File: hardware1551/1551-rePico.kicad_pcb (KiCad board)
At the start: 2 copper layers, 64.1 x 99.4 mm, 41 parts, among them J1 0.96_I2C_OLED, J10 TCBM, J11 JTAG, J6 Conn_01x05, J8 SD CARD, Q1 BSS138, Q2 BSS138, Q3 BSS138, Q4 BSS138, U1 Pico, U3 XC9572XL-VQ64, U4 6523 (pins), U5 6510T (pins), U6 6510T (socket for chip)

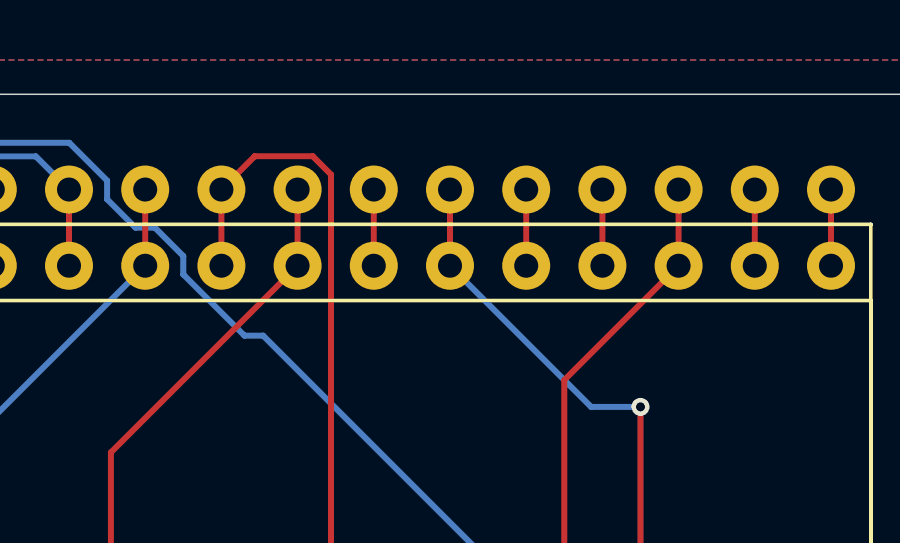
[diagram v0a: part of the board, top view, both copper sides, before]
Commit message: disconnect WPS from mainboard WPS becuase it's an output of U8 (pin2) that will keep it low with no mechanism present
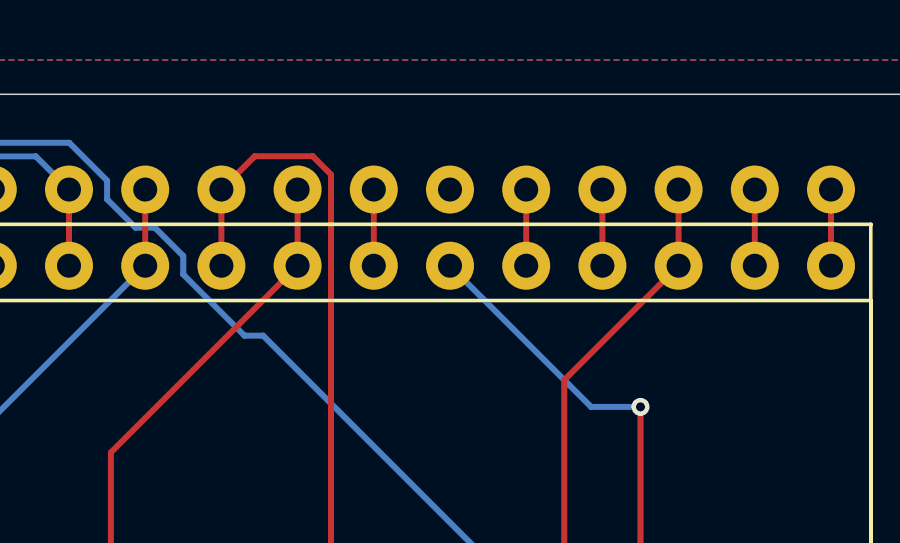
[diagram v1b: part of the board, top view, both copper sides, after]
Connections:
- U5 pad 26: /WPS -> unconnected-(U5-P4-Pad26)
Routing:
- net /WPS: track 40.9 -> 38.3 mm
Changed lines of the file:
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@@
 	(net 121 "Net-(JP5-A)")
 	(net 122 "/~{IRQ_BRD}")
+	(net 123 "unconnected-(U5-P4-Pad26)")
 	(footprint "Jumper:SolderJumper-3_P1.3mm_Bridged12_RoundedPad1.0x1.5mm_NumberLabels"
 		(layer "F.Cu")
@@
 			(layers "*.Cu" "*.Mask")
 			(remove_unused_layers no)
-			(net 41 "/WPS")
+			(net 123 "unconnected-(U5-P4-Pad26)")
 			(pinfunction "P4")
-			(pintype "bidirectional")
+			(pintype "bidirectional+no_connect")
 		)
 		(pad "27" thru_hole circle
@@
 		(width 0.2)
 		(layer "F.Cu")
-		(net 41)
-	)
-	(segment
-		(start 142.5956 68.5546)
-		(end 142.5956 66.0146)
-		(width 0.2)
-		(layer "F.Cu")

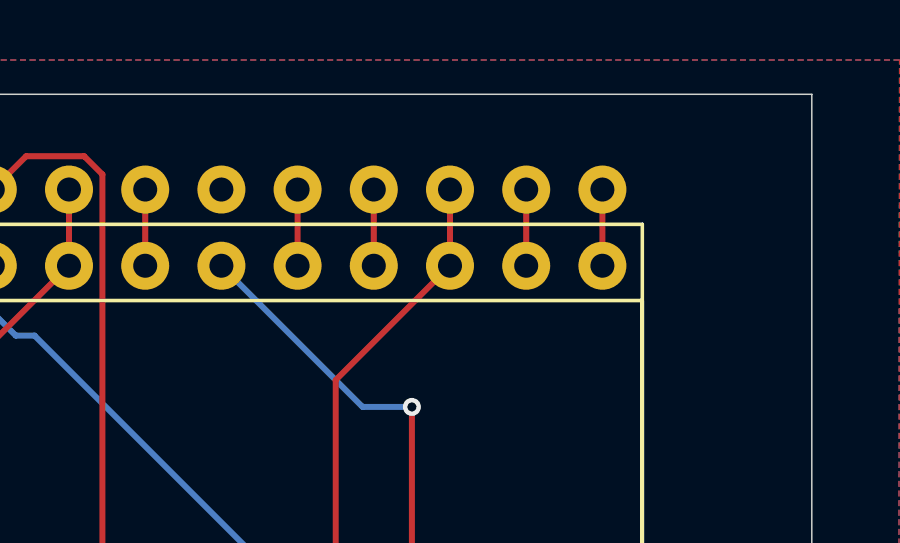
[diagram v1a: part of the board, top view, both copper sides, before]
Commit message: remove BYTE_LATCHED connection to the board, keep it only between CPU and CPLD
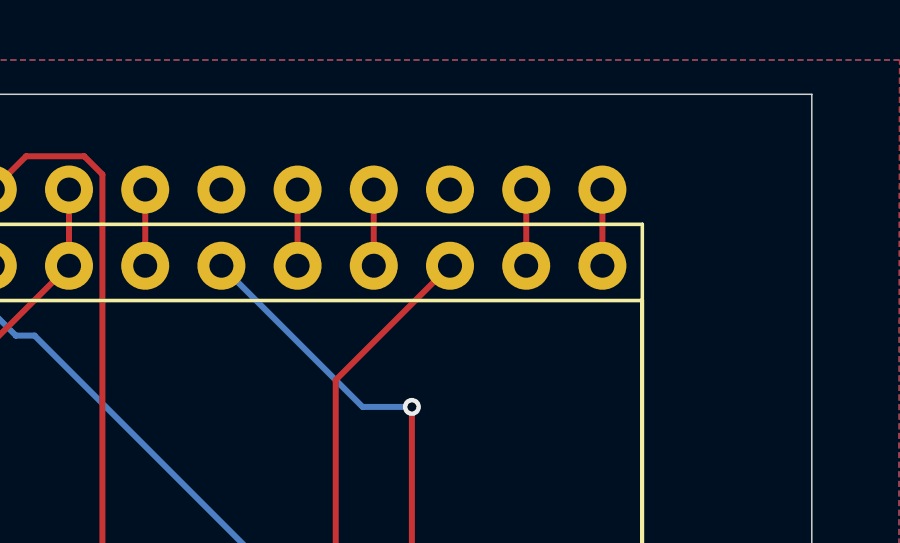
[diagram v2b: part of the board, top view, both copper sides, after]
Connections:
- U5 pad 23: /BYTE_LATCHED -> unconnected-(U5-P7-Pad23)
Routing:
- net /BYTE_LATCHED: track 62.5 -> 59.9 mm
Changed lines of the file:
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@@
 	(net 122 "/~{IRQ_BRD}")
 	(net 123 "unconnected-(U5-P4-Pad26)")
+	(net 124 "unconnected-(U5-P7-Pad23)")
 	(footprint "Jumper:SolderJumper-3_P1.3mm_Bridged12_RoundedPad1.0x1.5mm_NumberLabels"
 		(layer "F.Cu")
@@
 			(layers "*.Cu" "*.Mask")
 			(remove_unused_layers no)
-			(net 81 "/BYTE_LATCHED")
+			(net 124 "unconnected-(U5-P7-Pad23)")
 			(pinfunction "P7")
-			(pintype "bidirectional")
+			(pintype "bidirectional+no_connect")
 		)
 		(pad "24" thru_hole circle
@@
 		(width 0.2)
 		(layer "F.Cu")
-		(net 81)
-	)
-	(segment
-		(start 150.2156 68.5546)
-		(end 150.2156 66.0146)
-		(width 0.2)
-		(layer "F.Cu")
